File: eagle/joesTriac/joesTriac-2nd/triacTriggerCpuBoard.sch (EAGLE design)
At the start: 12 parts, among them IC2 LM311N, X1 87832-06

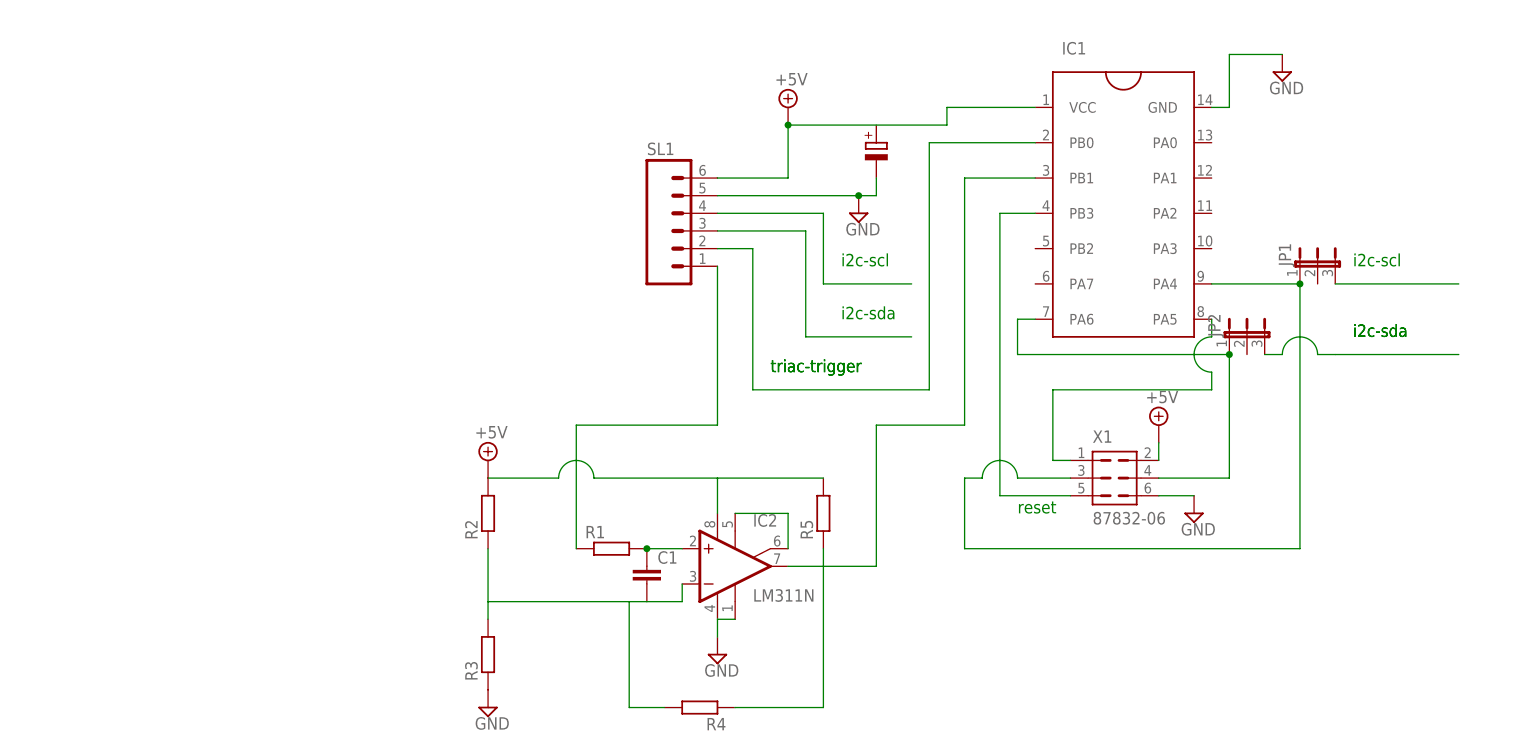
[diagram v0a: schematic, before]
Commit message: reg save, working on exti spikes
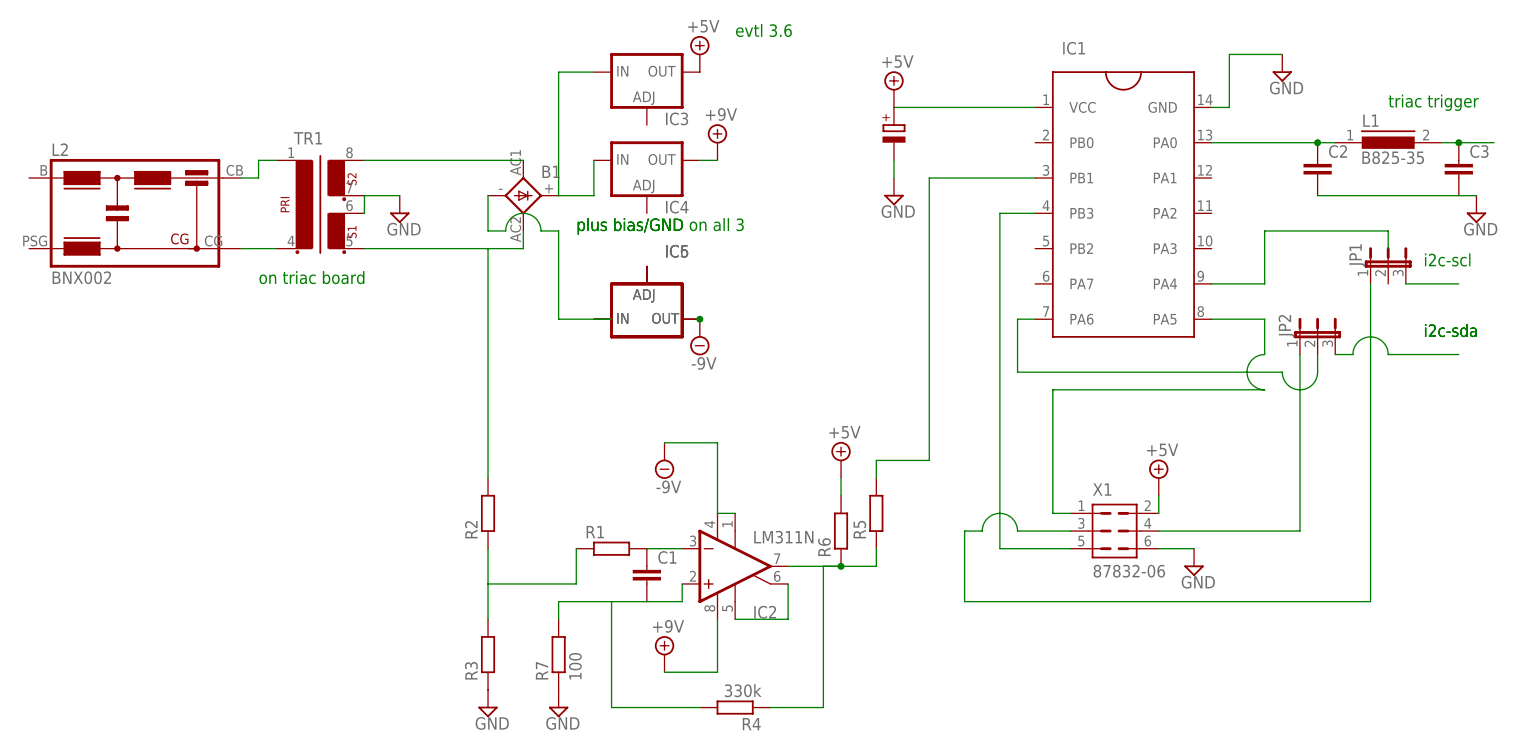
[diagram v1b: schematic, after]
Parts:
- removed SL1: (no value), con-amp-quick:M06
- added B1: (no value), rectifier:2KBB-R
- added C2, C3: (no value), capacitor-wima:C2,5-3
- added IC3, IC4: (no value), v-reg:LM317-TO3
- added IC5, IC6: (no value), v-reg:LM337TS
- added L1: B825-35, inductors:B825-35
- added L2: BNX002, inductors:BNX002
- added R6: (no value), resistor:R-EU_0207/10
- added R7: 100, resistor:R-EU_0207/10
- added TR1: (no value), trafo:EE20-2
- R4: value (none) -> 330k
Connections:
- removed net N$9 (its old number): IC1.PB0, SL1.2
- new net +9V: IC2.V+, IC4.OUT
- new net -9V: IC2.GND, IC2.V-, IC5.OUT, IC6.OUT
- new net N$15: IC2.OUT, R4.1, R5.1, R6.1
- new net N$16: IC5.ADJ, IC6.ADJ
- new net N$17: R1.1, R2.1, R3.2
- new net N$18: B1.+, IC3.IN, IC4.IN
- new net N$19: B1.-, IC5.IN, IC6.IN
- new net N$20: C2.1, IC1.PA0, L1.1
- new net N$21: IC1.PA4
- new net N$22: L2.CG, TR1.2
- new net N$23: L2.CB, TR1.1
- new net N$3: IC1.PA6, JP2.2
- net +5V: now also IC3.OUT, R6.2; no longer IC2.V+, R2.2, R5.2, SL1.6
- net GND: now also C2.2, R7.1, TR1.4, TR1.5; no longer IC2.GND, IC2.V-, SL1.5
- net N$10: now also C1.2, IC2.+IN, R4.2, R7.2; no longer R1.1, SL1.1
- net N$11: now also IC2.-IN; no longer IC2.+IN
- net N$12: now also C3.1, L1.2; no longer C1.2, IC2.-IN, R2.1, R3.2, R4.2
- net N$14: now also R5.2; no longer IC2.OUT, R4.1, R5.1
- net N$2: no longer IC1.PA6
- net N$5: no longer IC1.PA4
- net N$6: now also B1.AC2, R2.2, TR1.3; no longer SL1.3
- net N$8: now also B1.AC1, TR1.6; no longer SL1.4
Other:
- note added: "evtl 3.6"
- note added: "on triac board"
- note added: "plus bias/GND"
- note added: "plus bias/GND on all 3"
- note added: "triac trigger"
- note removed: "reset"
- note removed: "triac-trigger"
- moved on the sheet: IC2, JP1, JP2, R4, R5, X1

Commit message: candidate for release
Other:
- note added: "not implemented"
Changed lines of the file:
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@@
 <text x="68.58" y="101.6" size="1.778" layer="91">triac trigger</text>
 <text x="-25.4" y="111.76" size="1.778" layer="91">evtl 3.6</text>
+<text x="-119.38" y="106.68" size="5.08" layer="91">not implemented</text>
 </plain>
 <instances>
@@
 </segment>
 </net>
+<net name="N$24" class="0">
+<segment>
+<wire x1="-66.04" y1="104.14" x2="-119.38" y2="104.14" width="0.1524" layer="91"/>
+</segment>
+</net>
